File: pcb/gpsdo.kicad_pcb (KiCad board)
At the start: 4 copper layers, 120 x 100 mm, 151 parts, among them IC1 ICE40LP384-SG32, J1 JTAG, J10 CLK0, J11 CLK7, J12 USB_B_Micro, J13 CLK6, J14 CLK5, J15 CLK4, J2 SSD1306, J3 EXT_CLOCK, J4 GPS_ANT, J5 USB_B_Micro, J6 CLK3, J7 Screw_Terminal_01x03, J8 CLK2, J9 CLK1, M1 E73-2G4M08S1C-52840, Q1 S9018, SW1 EC11, SW2 MCML4-112B, U1 MCP9808_MSOP, U2 MCP9808_MSOP, U3 TPS652510, U4 LT1763xS8, U5 74LVC1G17, U6 Si5351C-B-GM, U7 74LVC1G17, U8 uBlox NEO-7M, U9 AD5761R, Y1 32768, Y2 8663-XS

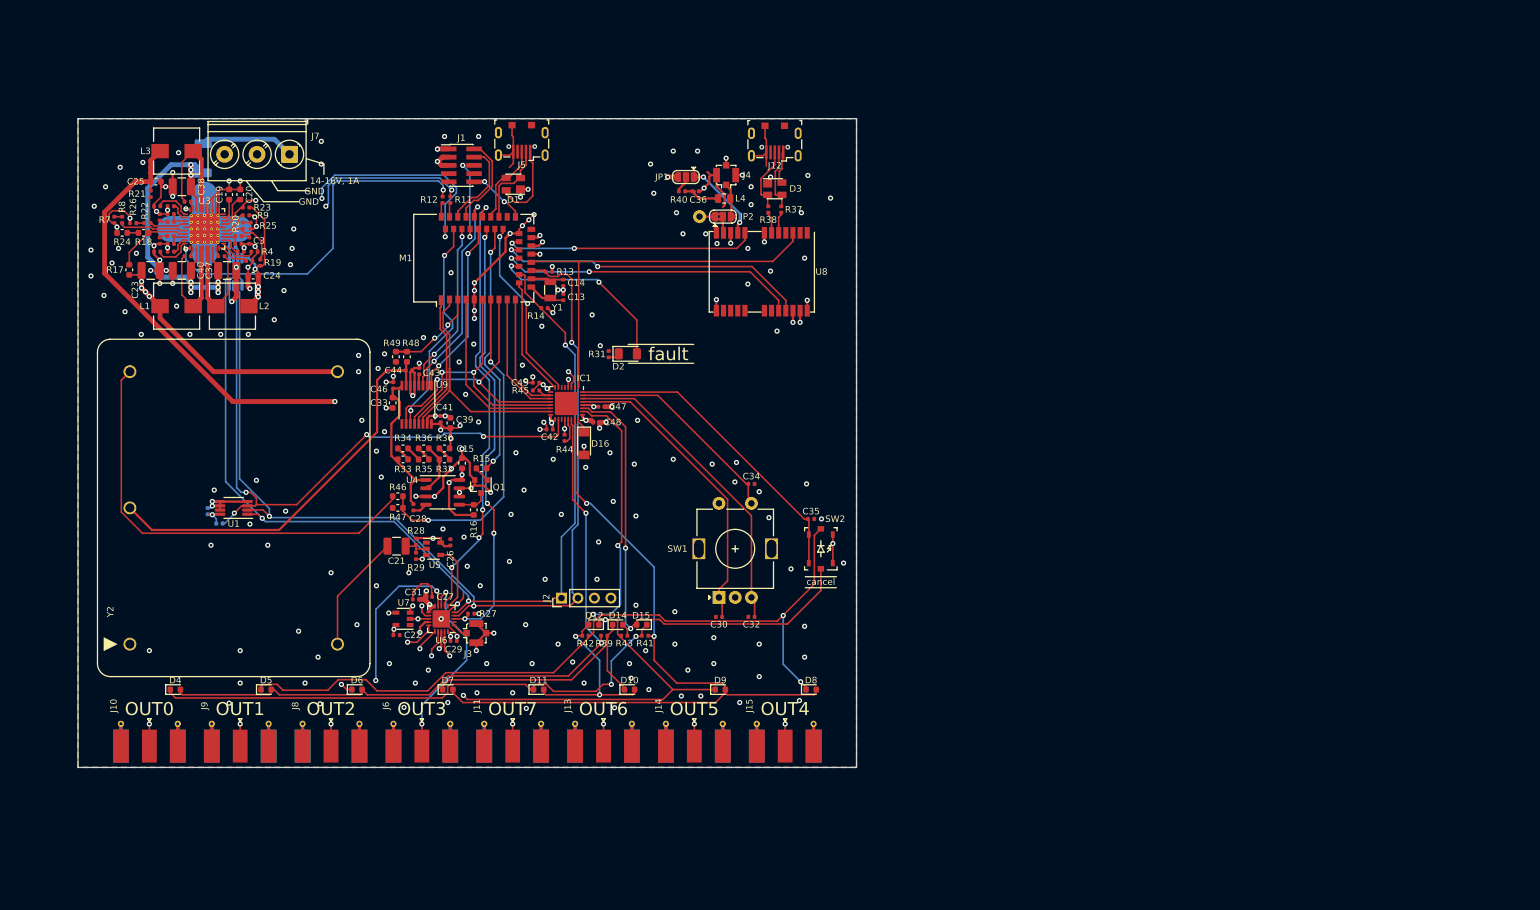
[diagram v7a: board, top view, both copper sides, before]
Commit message: add mounting holes, cleanup bord edge and mounting strategy. increase board size for that.
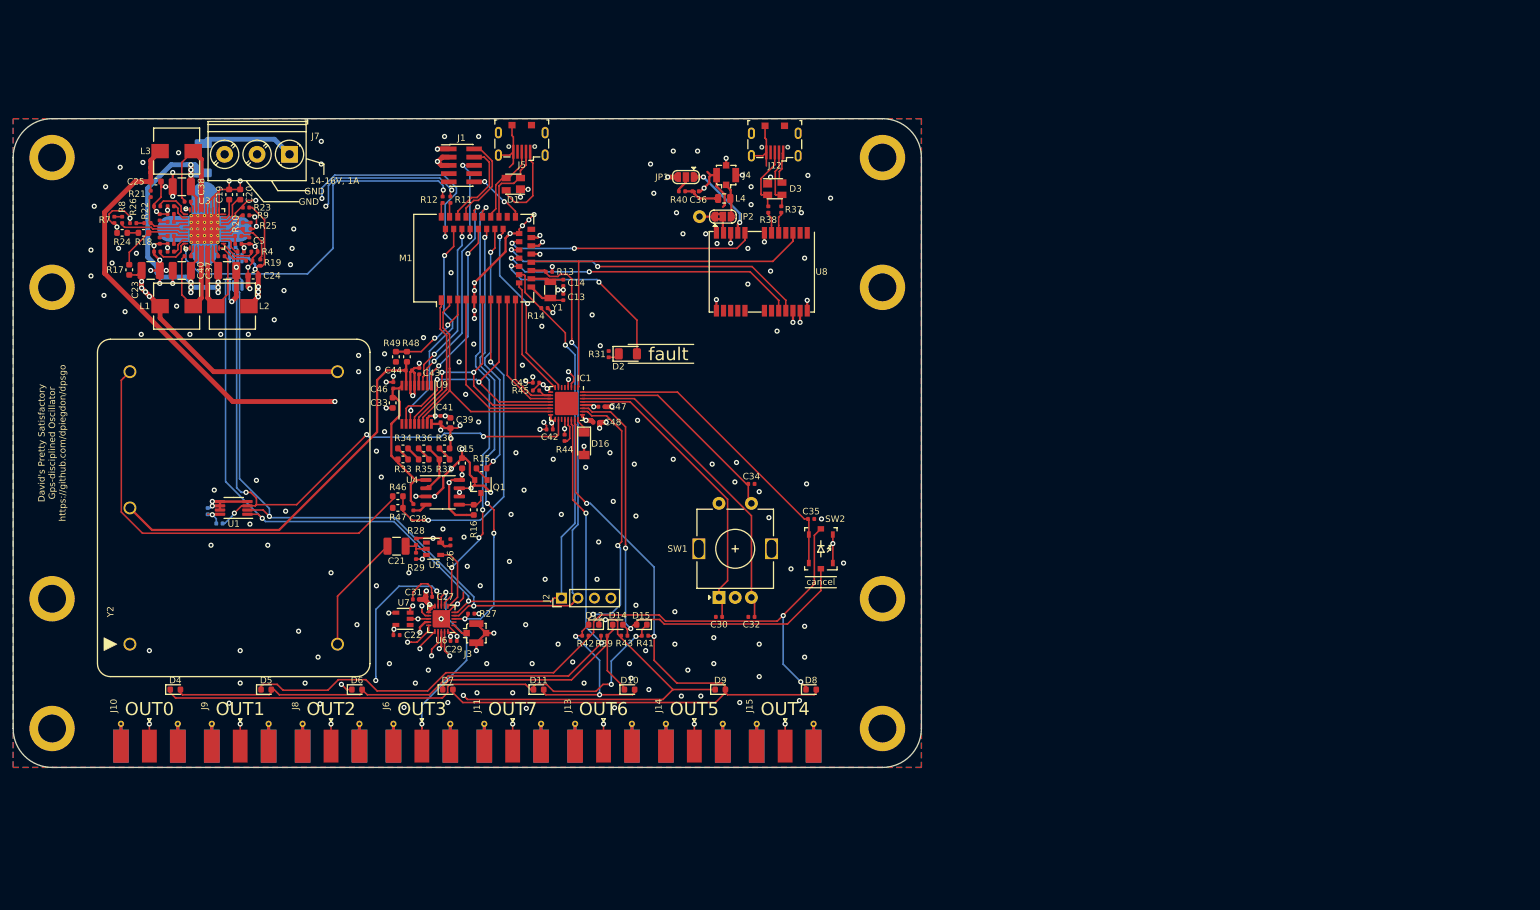
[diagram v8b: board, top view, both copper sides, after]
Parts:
- added H1: MountingHole, MountingHole:MountingHole_4.3mm_M4_ISO14580_Pad, F.Cu at (36.0, 46.0)
- added H2: MountingHole, MountingHole:MountingHole_4.3mm_M4_ISO14580_Pad, F.Cu at (36.0, 66.0)
- added H3: MountingHole, MountingHole:MountingHole_4.3mm_M4_ISO14580_Pad, F.Cu at (164.0, 46.0)
- added H4: MountingHole, MountingHole:MountingHole_4.3mm_M4_ISO14580_Pad, F.Cu at (164.0, 66.0)
- added H5: MountingHole, MountingHole:MountingHole_4.3mm_M4_ISO14580_Pad, F.Cu at (36.0, 114.0)
- added H6: MountingHole, MountingHole:MountingHole_4.3mm_M4_ISO14580_Pad, F.Cu at (36.0, 134.0)
- added H7: MountingHole, MountingHole:MountingHole_4.3mm_M4_ISO14580_Pad, F.Cu at (164.0, 114.0)
- added H8: MountingHole, MountingHole:MountingHole_4.3mm_M4_ISO14580_Pad, F.Cu at (164.0, 134.0)
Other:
- board size 120 x 100 mm -> 140 x 100 mm
- board text added: "David's Pretty Satisfactory Gps-disciplined Oscillator https://github.com/dpiegdon/dpsgo"
